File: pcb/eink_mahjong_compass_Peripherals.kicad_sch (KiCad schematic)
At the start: 31 parts, among them J1 PH-2AWT, J2 Touch1, J3 Touch2, J4 Touch3, J5 Touch4, SW3 C318884, SW4 C318884, SW5 C318884, SW6 C318884, U1 C16581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

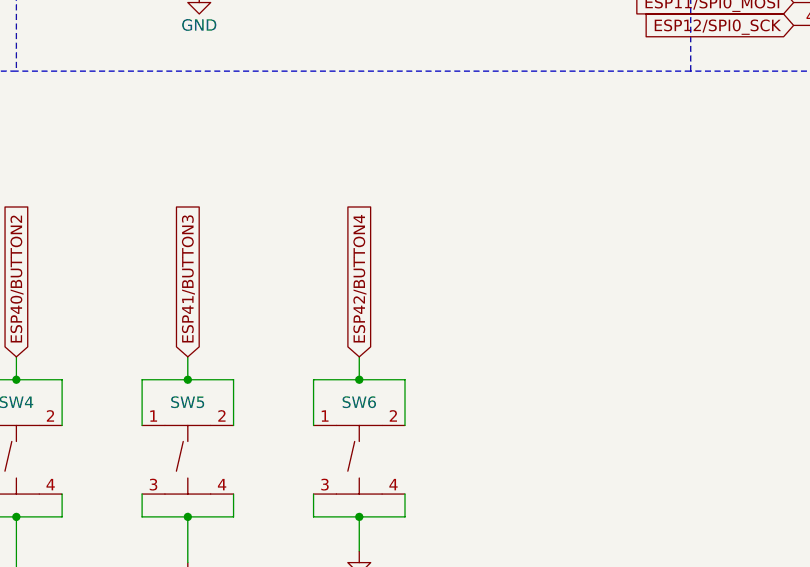
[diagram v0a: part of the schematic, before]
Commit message: pcb: add missing trace to make deep sleep wakeup work
Connect button 4 for gpio 3 as well, so it can be used to wake up the
esp32 from deep sleep as the gpios selected for the buttons don't have
that capability.
In a future revision this should be redesigned so all buttons can act as
wakeup trigger.
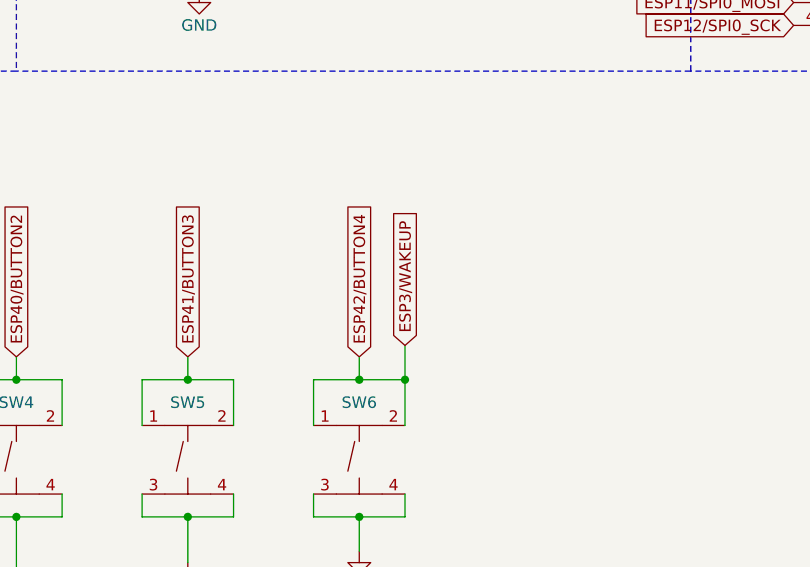
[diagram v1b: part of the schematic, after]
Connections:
- net ESP42/BUTTON4 renamed ESP3/WAKEUP
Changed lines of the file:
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@@
+	)
+	(junction
+		(at 158.75 165.1)
+		(diameter 0)
+		(color 0 0 0 0)
 	)
 	(junction
@@
 		(pts
 			(xy 137.16 52.07) (xy 149.86 52.07)
+		)
+		(stroke
+			(width 0)
+			(type default)
+		)
+	)
+	(wire
+		(pts
+			(xy 158.75 161.29) (xy 158.75 165.1)
 		)
 		(stroke
@@
 			(hide yes)
 			(show_name no)
+			(do_not_autoplace no)
+			(effects
+				(font
+					(size 1.27 1.27)
+				)
+				(justify left)
+			)
+		)
+	)
+	(global_label "ESP3{slash}WAKEUP"
+		(shape input)
+		(at 158.75 161.29 90)
+		(fields_autoplaced yes)
+		(effects
+			(font
+				(size 1.27 1.27)
+			)
+			(justify left)
+		)
+		(property "Intersheetrefs" "${INTERSHEET_REFS}"
+			(at 158.75 144.5768 90)
+			(hide yes)
+			(show_name no)
